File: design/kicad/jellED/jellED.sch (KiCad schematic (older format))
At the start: 7 parts

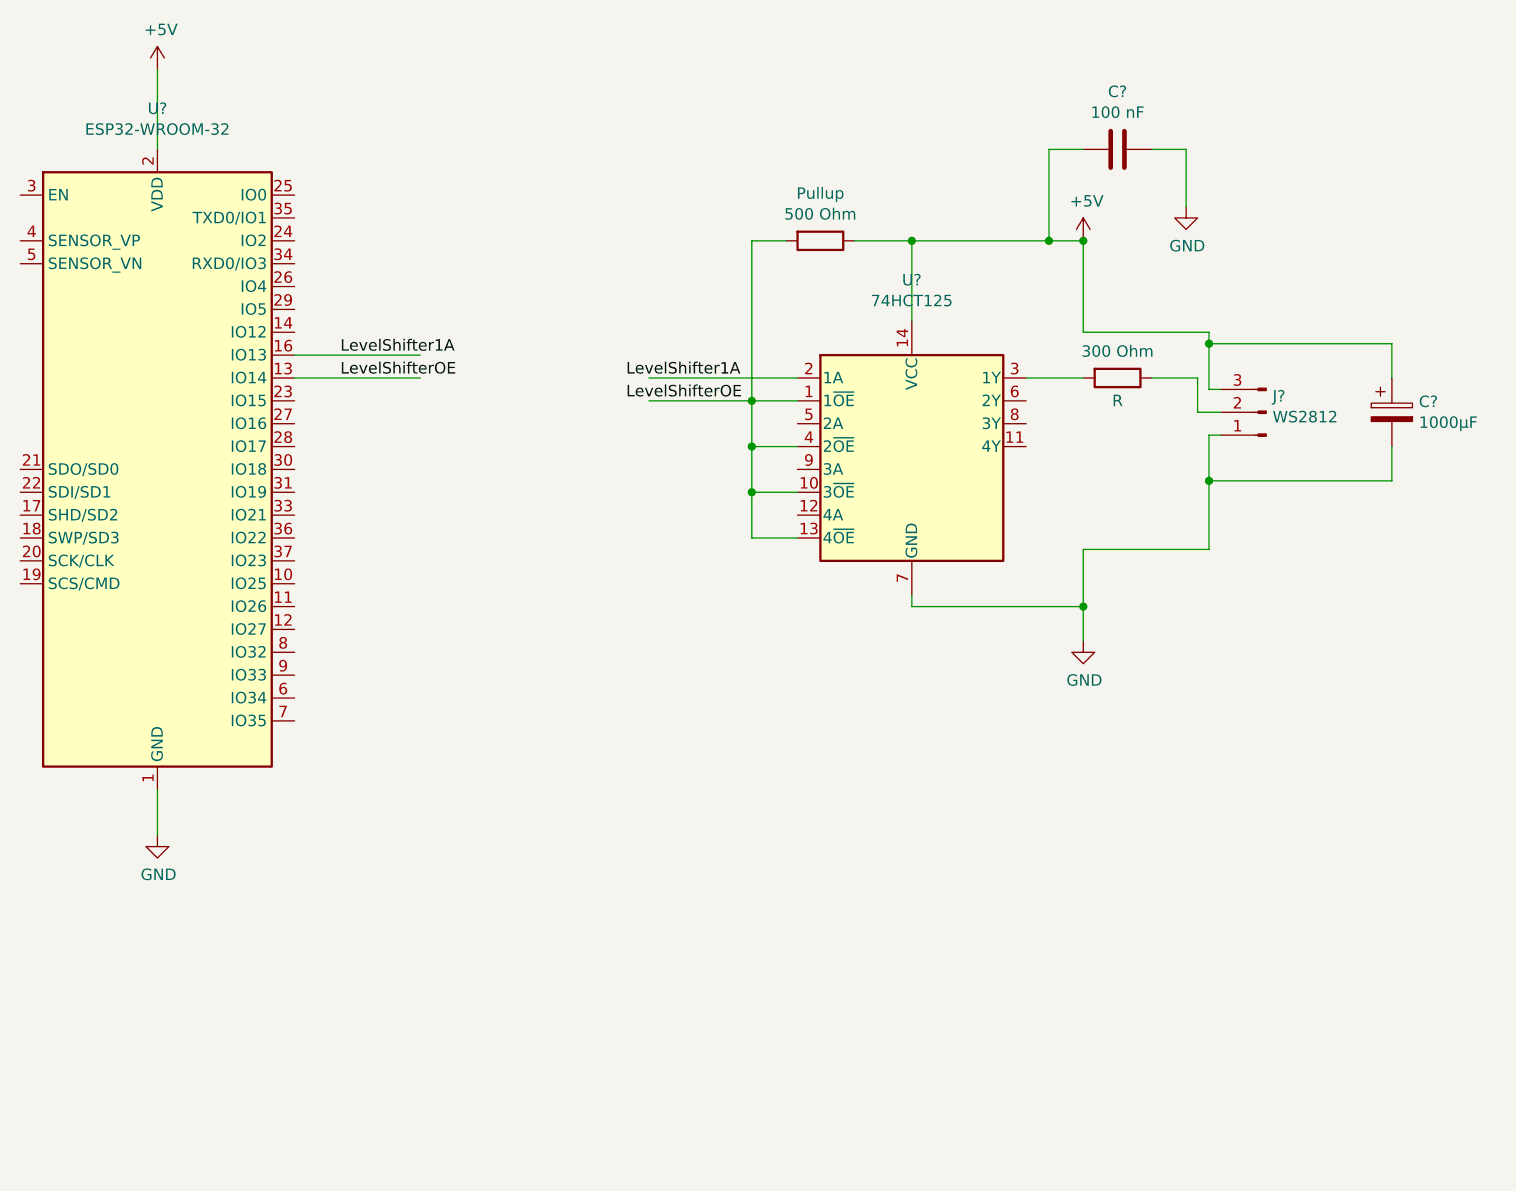
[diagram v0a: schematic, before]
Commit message: Adds INMP441 microphone
Adds library and design for the INMP441 microphone to read sound data
via the ESP32's I2c port
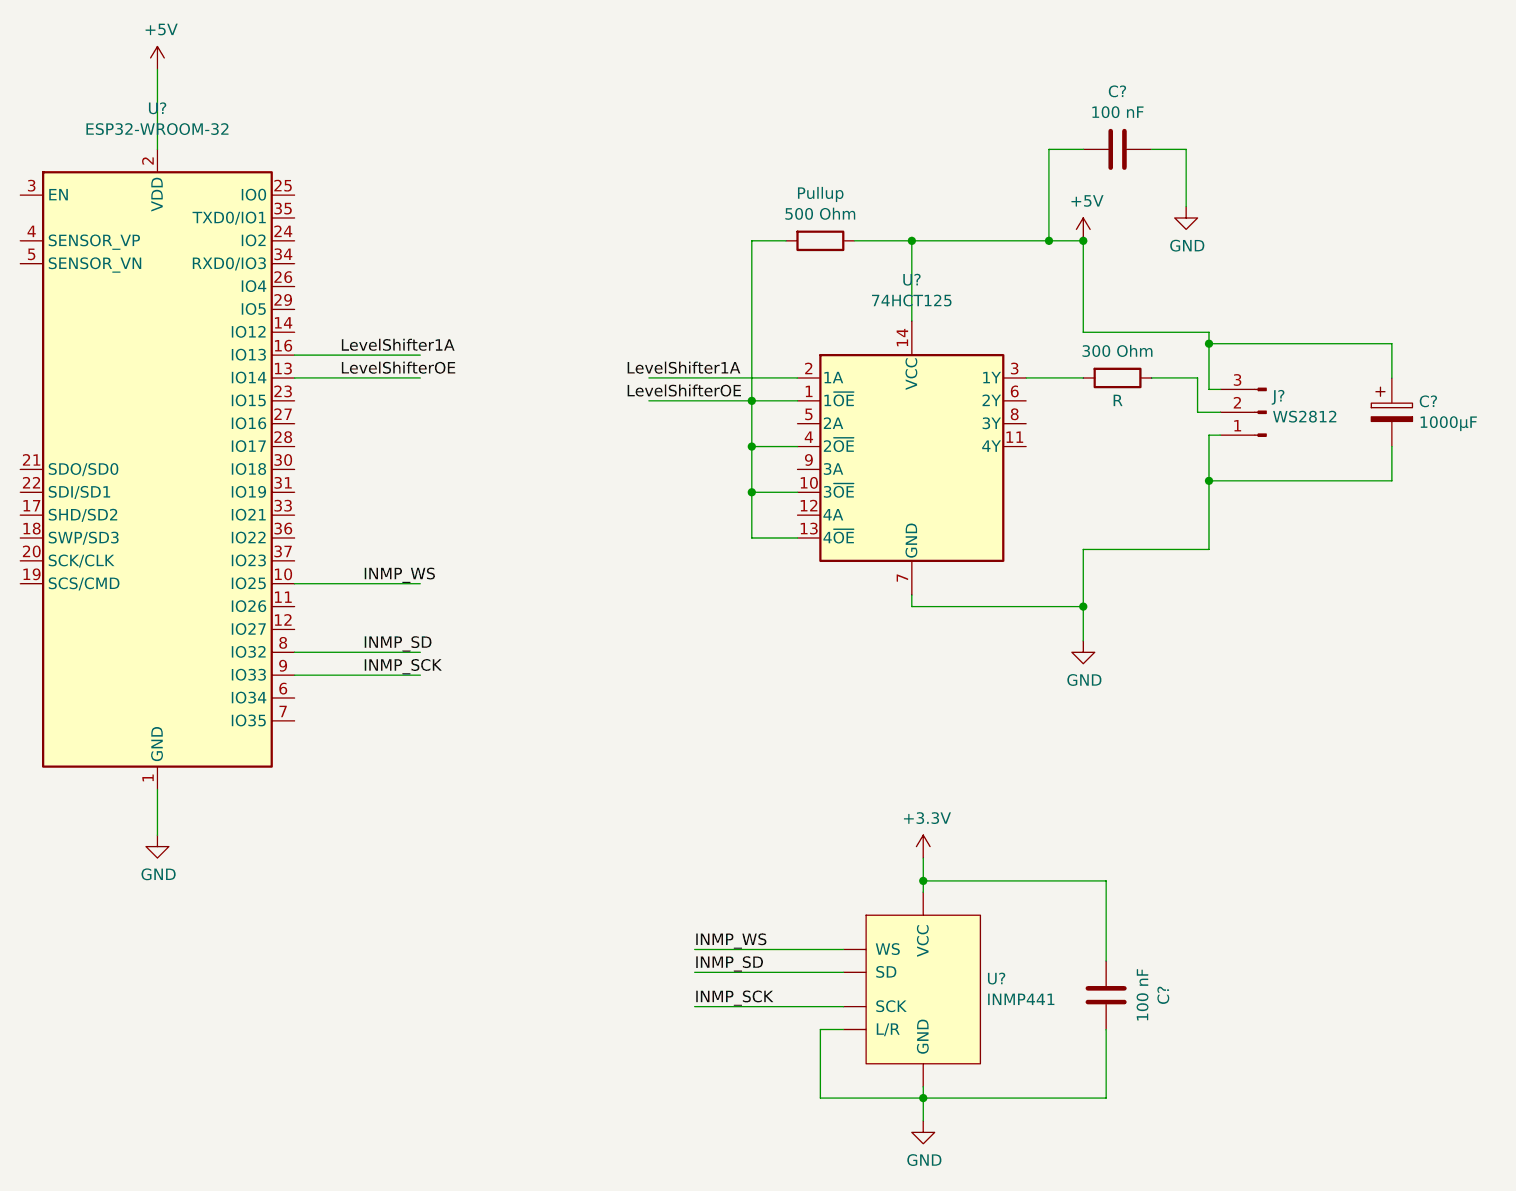
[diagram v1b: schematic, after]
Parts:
- added C?: 100 nF, symbol Device:C
- added U?: INMP441, symbol INMP441:INMP441
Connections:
- net labels added: +3.3V, INMP_SCK, INMP_SD, INMP_WS
- wire segments 44 -> 61
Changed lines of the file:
@@
 Text Label 3400 2100 0    50   ~ 0
 LevelShifterOE
+$Comp
+L INMP441:INMP441 U?
+U 1 1 64D11D1A
+P 5950 4750
+F 0 "U?" H 6227 4771 50  0000 L CNN
+F 1 "INMP441" H 6227 4680 50  0000 L CNN
+F 2 "" H 5950 4750 50  0001 C CNN
+F 3 "" H 5950 4750 50  0001 C CNN
+	1    5950 4750
+	1    0    0    -1
+$EndComp
+$Comp
+L power:GND #PWR?
+U 1 1 64D12791
+P 5950 5350
+F 0 "#PWR?" H 5950 5100 50  0001 C CNN
+F 1 "GND" H 5955 5177 50  0000 C CNN
+F 2 "" H 5950 5350 50  0001 C CNN
+F 3 "" H 5950 5350 50  0001 C CNN
+	1    5950 5350
+	1    0    0    -1
+$EndComp
+$Comp
+L power:+3.3V #PWR?
+U 1 1 64D12869
+P 5950 4200
+F 0 "#PWR?" H 5950 4050 50  0001 C CNN
+F 1 "+3.3V" H 5965 4373 50  0000 C CNN
+F 2 "" H 5950 4200 50  0001 C CNN
+F 3 "" H 5950 4200 50  0001 C CNN
+	1    5950 4200
+	1    0    0    -1
+$EndComp
+Wire Wire Line
+	5950 4350 5950 4300
+Wire Wire Line
+	5950 5350 5950 5250
+Wire Wire Line
+	5600 4950 5500 4950
+Wire Wire Line
+	5500 4950 5500 5250
+Wire Wire Line
+	5500 5250 5950 5250
+Connection ~ 5950 5250
+Wire Wire Line
+	5950 5250 5950 5200
+Wire Wire Line
+	5600 4600 4950 4600
+Wire Wire Line
+	5600 4700 4950 4700
+Wire Wire Line
+	5600 4850 4950 4850
+Text Label 4950 4600 0    50   ~ 0
+INMP_WS
+Text Label 4950 4700 0    50   ~ 0
+INMP_SD
+Text Label 4950 4850 0    50   ~ 0
+INMP_SCK
+$Comp
+L Device:C C?
+U 1 1 64D16128
+P 6750 4800
+F 0 "C?" V 6498 4800 50  0000 C CNN
+F 1 "100 nF" V 6589 4800 50  0000 C CNN
+F 2 "" H 6788 4650 50  0001 C CNN
+F 3 "~" H 6750 4800 50  0001 C CNN
+	1    6750 4800
+	-1   0    0    1
+$EndComp
+Wire Wire Line
+	5950 4300 6750 4300
+Wire Wire Line
+	6750 4300 6750 4650
+Connection ~ 5950 4300
+Wire Wire Line
+	5950 4300 5950 4200
+Wire Wire Line
+	6750 4950 6750 5250
+Wire Wire Line
+	6750 5250 5950 5250
+Wire Wire Line
+	3200 3000 3750 3000
+Wire Wire Line
+	3200 3300 3750 3300
+Wire Wire Line
+	3200 3400 3750 3400
+Text Label 3500 3000 0    50   ~ 0
+INMP_WS
+Text Label 3500 3300 0    50   ~ 0
+INMP_SD
+Text Label 3500 3400 0    50   ~ 0
+INMP_SCK
 $EndSCHEMATC
